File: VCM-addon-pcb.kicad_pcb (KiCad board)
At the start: 2 copper layers, 40.7 x 29.6 mm, 5 parts, among them U1 DRV8210

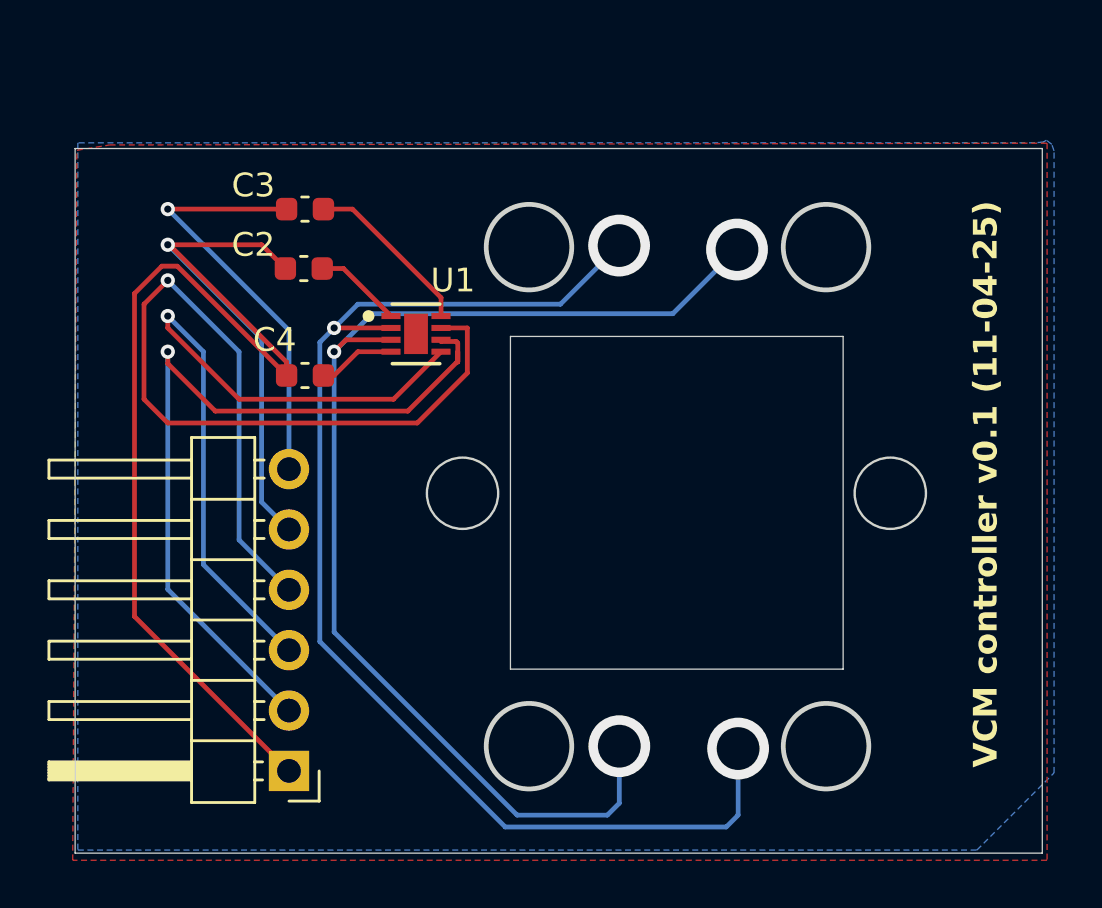
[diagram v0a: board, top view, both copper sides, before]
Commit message: fixes after paper check, DRC passed + Gerber ZIP
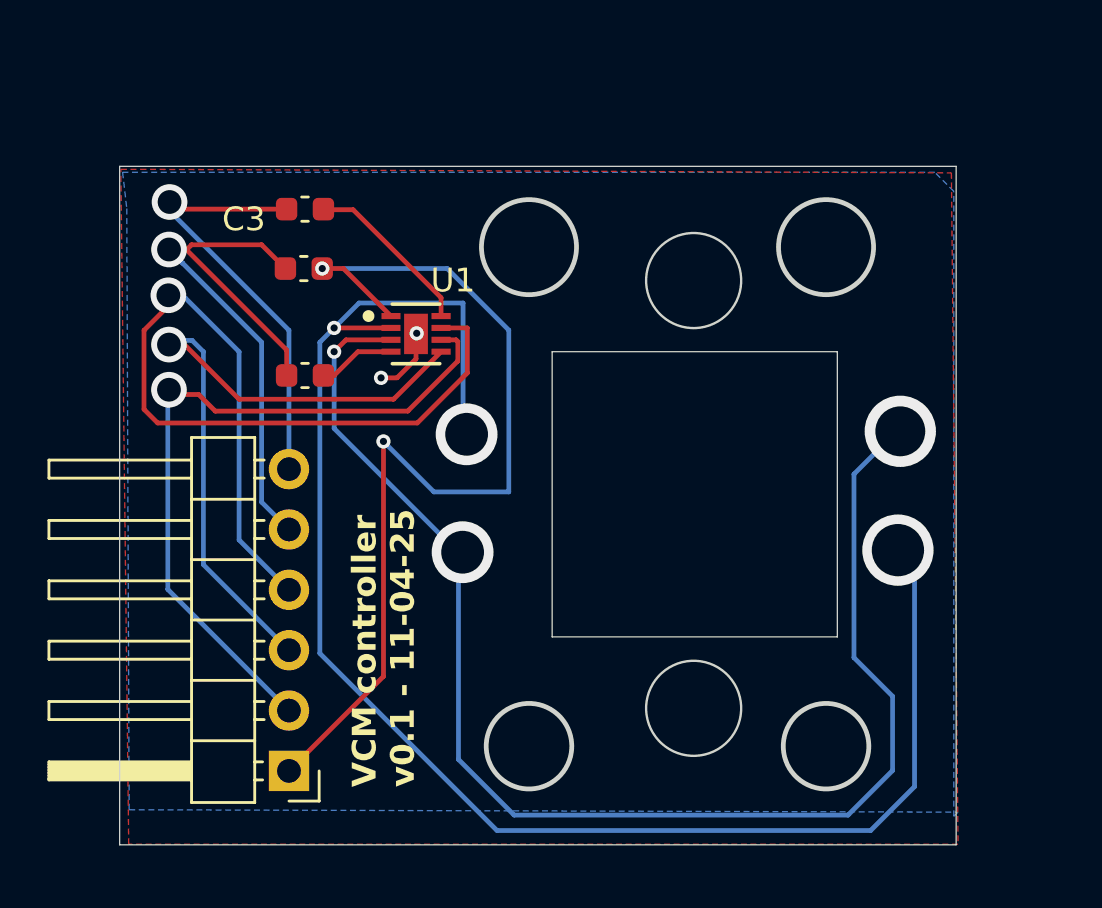
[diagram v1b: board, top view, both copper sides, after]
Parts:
- C2, C3, C4: footprint drv8210:C_0603_1608Metric -> Capacitor_SMD:C_0603_1608Metric
- U1: value DRV8210 -> DRV8210DSGR
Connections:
- .54mm_Haaks pad 1: GNDREF -> Net-(U1-VM)
- .54mm_Haaks pad 6: Net-(U1-VCC) -> +3.3V
- C3 pad 1: Net-(U1-VCC) -> +3.3V
- U1 pad 9: unconnected-(U1-Thermal_Pad-Pad9) -> GNDREF
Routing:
- net Net-(U1-VM): track 3.72 -> 41.1 mm, vias 0 -> 2
- net GNDREF: track 58.6 -> 29.9 mm, vias 1 -> 3
- net Net-(U1-VCC): track 25.3 -> 7.54 mm, vias 1 -> 0
- net +3.3V: track 0.00 -> 17.8 mm, vias 0 -> 1
- net VCM -: track 53.3 -> 67.1 mm
- net VCM +: track 50.9 -> 57.6 mm
- net PWM_PH: track 33.6 -> 30.6 mm
- net PWM_EN: track 30.2 -> 29.1 mm
- net SLEEP: track 38.4 -> 37.9 mm
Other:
- board size 40.7 x 29.6 mm -> 35.2 x 28.5 mm
- board text added: "VCM controller v0.1 - 11-04-25"
- board text removed: "VCM controller v0.1 (11-04-25)"
